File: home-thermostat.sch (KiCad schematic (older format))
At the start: 49 parts

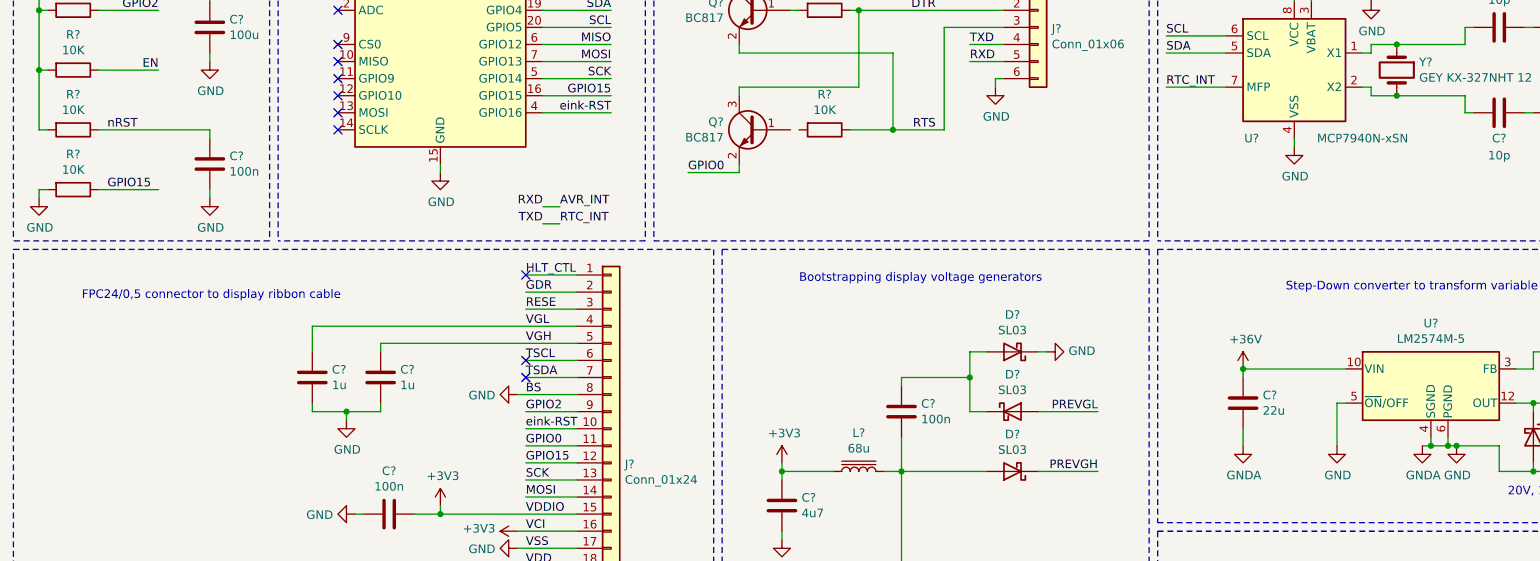
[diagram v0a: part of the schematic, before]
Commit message: Added footprints to most symbols.
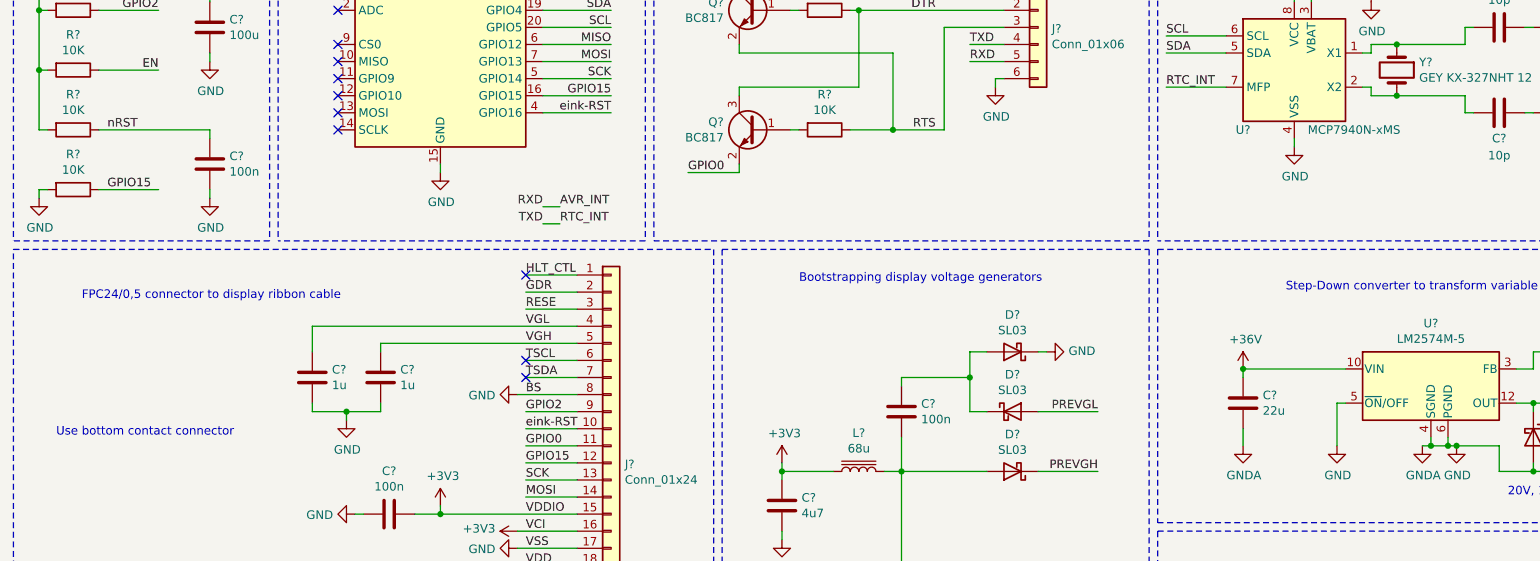
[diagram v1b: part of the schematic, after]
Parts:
- removed U?: MCP7940N-xSN, symbol Timer:MCP7940N-xSN
- added U?: MCP7940N-xMS, Package_SO:MSOP-8_3x3mm_P0.65mm, symbol Timer:MCP7940N-xMS
- D? (x4): footprint (none) -> Diode_SMD:D_SMF
- Q? (x3): footprint (none) -> Package_TO_SOT_SMD:SOT-23
- R? (x9): footprint (none) -> Resistor_SMD:R_0603_1608Metric
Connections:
- net +3V3: now also U?.8 (VCC)
- net GND: now also U?.4 (VSS)
- net RTC_INT: now also U?.7 (MFP)
- net SCL: now also U?.6 (SCL)
- net SDA: now also U?.5 (SDA)
- net at C?.2, Y?.1: now also U?.1 (X1)
- net at C?.2, Y?.2: now also U?.2 (X2)
- net at BT?.1 (+): now also U?.3 (VBAT)
- net at R?.2: now also Q?.1 (B)
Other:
- note added: "Use bottom contact connector"
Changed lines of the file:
@@
 F 0 "R?" V 5043 2100 50  0000 C CNN
 F 1 "10K" V 5134 2100 50  0000 C CNN
-F 2 "" V 5180 2100 50  0001 C CNN
+F 2 "Resistor_SMD:R_0603_1608Metric" V 5180 2100 50  0001 C CNN
 F 3 "~" H 5250 2100 50  0001 C CNN
 	1    5250 2100
@@
 F 0 "R?" V 5043 1400 50  0000 C CNN
 F 1 "10K" V 5134 1400 50  0000 C CNN
-F 2 "" V 5180 1400 50  0001 C CNN
+F 2 "Resistor_SMD:R_0603_1608Metric" V 5180 1400 50  0001 C CNN
 F 3 "~" H 5250 1400 50  0001 C CNN
 	1    5250 1400
@@
 $EndComp
 $Comp
-L Timer:MCP7940N-xSN U?
-U 1 1 5E93A4D3
-P 8000 1750
-AR Path="/5E9313E4/5E93A4D3" Ref="U?"  Part="1"
-AR Path="/5E93A4D3" Ref="U?"  Part="1"
-F 0 "U?" H 7750 1350 50  0000 C CNN
-F 1 "MCP7940N-xSN" H 8400 1350 50  0000 C CNN
-F 2 "" H 8000 1750 50  0001 C CNN
-F 3 "http://ww1.microchip.com/downloads/en/DeviceDoc/20005010F.pdf" H 8000 1750 50  0001 C CNN
-	1    8000 1750
-	1    0    0    -1
-$EndComp
-$Comp
 L power:GND #PWR0108
 U 1 1 5E5B5397
@@
 F 0 "R?" V 643 2450 50  0000 C CNN
 F 1 "10K" V 734 2450 50  0000 C CNN
-F 2 "" V 780 2450 50  0001 C CNN
+F 2 "Resistor_SMD:R_0603_1608Metric" V 780 2450 50  0001 C CNN
 F 3 "~" H 850 2450 50  0001 C CNN
 	1    850  2450
@@
 F 0 "R?" V 643 2100 50  0000 C CNN
 F 1 "10K" V 734 2100 50  0000 C CNN
-F 2 "" V 780 2100 50  0001 C CNN
+F 2 "Resistor_SMD:R_0603_1608Metric" V 780 2100 50  0001 C CNN
 F 3 "~" H 850 2100 50  0001 C CNN
 	1    850  2100
@@
 F 0 "R?" V 643 1750 50  0000 C CNN
 F 1 "10K" V 734 1750 50  0000 C CNN
-F 2 "" V 780 1750 50  0001 C CNN
+F 2 "Resistor_SMD:R_0603_1608Metric" V 780 1750 50  0001 C CNN
 F 3 "~" H 850 1750 50  0001 C CNN
 	1    850  1750
@@
 F 0 "R?" V 643 1400 50  0000 C CNN
 F 1 "10K" V 734 1400 50  0000 C CNN
-F 2 "" V 780 1400 50  0001 C CNN
+F 2 "Resistor_SMD:R_0603_1608Metric" V 780 1400 50  0001 C CNN
 F 3 "~" H 850 1400 50  0001 C CNN
 	1    850  1400
@@
 F 0 "R?" V 1057 1050 50  0000 C CNN
 F 1 "10K" V 966 1050 50  0000 C CNN
-F 2 "" V 780 1050 50  0001 C CNN
+F 2 "Resistor_SMD:R_0603_1608Metric" V 780 1050 50  0001 C CNN
 F 3 "~" H 850 1050 50  0001 C CNN
 	1    850  1050
@@
 F 0 "Q?" H 5041 1446 50  0000 L CNN
 F 1 "BC817" H 5041 1355 50  0000 L CNN
-F 2 "" H 5050 1500 50  0001 C CNN
+F 2 "Package_TO_SOT_SMD:SOT-23" H 5050 1500 50  0001 C CNN
 F 3 "https://www.mouser.de/datasheet/2/916/BC817_SER-1598763.pdf" H 4850 1400 50  0001 C CNN
 	1    4850 1400
@@
 F 0 "Q?" H 5041 2146 50  0000 L CNN
 F 1 "BC817" H 5041 2055 50  0000 L CNN
-F 2 "" H 5050 2200 50  0001 C CNN
+F 2 "Package_TO_SOT_SMD:SOT-23" H 5050 2200 50  0001 C CNN
 F 3 "https://www.mouser.de/datasheet/2/916/BC817_SER-1598763.pdf" H 4850 2100 50  0001 C CNN
 	1    4850 2100
@@
 F 0 "D?" V 9354 3980 50  0000 L CNN
 F 1 "SL03" V 9445 3980 50  0000 L CNN
-F 2 "" H 9400 3900 50  0001 C CNN
+F 2 "Diode_SMD:D_SMF" H 9400 3900 50  0001 C CNN
 F 3 "~" H 9400 3900 50  0001 C CNN
 	1    9400 3900
@@
 F 0 "R?" H 5070 5446 50  0000 L CNN
 F 1 "10K" H 5070 5355 50  0000 L CNN
-F 2 "" V 4930 5400 50  0001 C CNN
+F 2 "Resistor_SMD:R_0603_1608Metric" V 4930 5400 50  0001 C CNN
 F 3 "~" H 5000 5400 50  0001 C CNN
 	1    5000 5400
@@
 F 0 "R?" H 5770 5446 50  0000 L CNN
 F 1 "0.47R" H 5770 5355 50  0000 L CNN
-F 2 "" V 5630 5400 50  0001 C CNN
+F 2 "Resistor_SMD:R_0603_1608Metric" V 5630 5400 50  0001 C CNN
 F 3 "~" H 5700 5400 50  0001 C CNN
 	1    5700 5400
@@
 F 0 "D?" H 6350 3967 50  0000 C CNN
 F 1 "SL03" H 6350 3876 50  0000 C CNN
-F 2 "" H 6350 3750 50  0001 C CNN
+F 2 "Diode_SMD:D_SMF" H 6350 3750 50  0001 C CNN
 F 3 "~" H 6350 3750 50  0001 C CNN
 	1    6350 3750
@@
 F 0 "D?" H 6350 3183 50  0000 C CNN
 F 1 "SL03" H 6350 3274 50  0000 C CNN
-F 2 "" H 6350 3400 50  0001 C CNN
+F 2 "Diode_SMD:D_SMF" H 6350 3400 50  0001 C CNN
 F 3 "~" H 6350 3400 50  0001 C CNN
 	1    6350 3400
@@
 F 0 "D?" H 6350 3883 50  0000 C CNN
 F 1 "SL03" H 6350 3974 50  0000 C CNN
-F 2 "" H 6350 4100 50  0001 C CNN
+F 2 "Diode_SMD:D_SMF" H 6350 4100 50  0001 C CNN
 F 3 "~" H 6350 4100 50  0001 C CNN
 	1    6350 4100
@@
 F 0 "Q?" H 5805 4896 50  0000 L CNN
 F 1 "BSS806NL6327" H 5805 4805 50  0000 L CNN
-F 2 "" H 5800 4950 50  0001 C CNN
+F 2 "Package_TO_SOT_SMD:SOT-23" H 5800 4950 50  0001 C CNN
 F 3 "~" H 5600 4850 50  0001 C CNN
 	1    5600 4850
@@
 Wire Wire Line
 	9350 5150 9950 5150
+Text Notes 750  3900 0    50   ~ 0
+Use bottom contact connector
+$Comp
+L Timer:MCP7940N-xMS U?
+U 1 1 5F13EEA2
+P 8000 1750
+F 0 "U?" H 7700 1400 50  0000 C CNN
+F 1 "MCP7940N-xMS" H 8350 1400 50  0000 C CNN
+F 2 "Package_SO:MSOP-8_3x3mm_P0.65mm" H 8000 1750 50  0001 C CNN
+F 3 "http://ww1.microchip.com/downloads/en/DeviceDoc/20005010F.pdf" H 8000 1750 50  0001 C CNN
+	1    8000 1750
+	1    0    0    -1
+$EndComp
+Wire Wire Line
+	5100 2100 5050 2100
 $EndSCHEMATC

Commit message: Added all footprints except for ones which I have to look up in the E-Lab.
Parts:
- J?: footprint (none) -> Connector_PinHeader_2.54mm:PinHeader_2x03_P2.54mm_Vertical_SMD
- J?: footprint (none) -> Connector_PinHeader_2.54mm:PinHeader_1x03_P2.54mm_Vertical_SMD_Pin1Left
- L?: footprint (none) -> Inductor_SMD:L_7.3x7.3_H3.5
- L?: footprint (none) -> Inductor_SMD:L_1210_3225Metric
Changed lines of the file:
@@
 F 0 "J?" H 6580 1492 50  0000 L CNN
 F 1 "Conn_01x06" H 6580 1401 50  0000 L CNN
-F 2 "" H 6500 1500 50  0001 C CNN
+F 2 "Connector_PinHeader_2.54mm:PinHeader_2x03_P2.54mm_Vertical_SMD" H 6500 1500 50  0001 C CNN
 F 3 "~" H 6500 1500 50  0001 C CNN
 	1    6500 1500
@@
 F 0 "J?" H 3330 6542 50  0000 L CNN
 F 1 "Thermosthat" H 3330 6451 50  0000 L CNN
-F 2 "" H 3250 6500 50  0001 C CNN
+F 2 "Connector_PinHeader_2.54mm:PinHeader_1x03_P2.54mm_Vertical_SMD_Pin1Left" H 3250 6500 50  0001 C CNN
 F 3 "~" H 3250 6500 50  0001 C CNN
 	1    3250 6500
@@
 F 0 "L?" V 9975 3700 50  0000 C CNN
 F 1 "330u" V 9884 3700 50  0000 C CNN
-F 2 "" H 9750 3700 50  0001 C CNN
+F 2 "Inductor_SMD:L_7.3x7.3_H3.5" H 9750 3700 50  0001 C CNN
 F 3 "~" H 9750 3700 50  0001 C CNN
 	1    9750 3700
@@
 F 0 "L?" V 5675 4100 50  0000 C CNN
 F 1 "68u" V 5584 4100 50  0000 C CNN
-F 2 "" H 5450 4100 50  0001 C CNN
+F 2 "Inductor_SMD:L_1210_3225Metric" H 5450 4100 50  0001 C CNN
 F 3 "~" H 5450 4100 50  0001 C CNN
 	1    5450 4100
